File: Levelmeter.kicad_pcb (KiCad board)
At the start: 4 copper layers, 90 x 70 mm, 140 parts, among them J1 JST_PH_2.0mm_1x02, J2 USB_C, J4 Header_50mil_2x07, J5 Header_100mil_1x06, J6 Header_100mil_1x06, J7 JST_PH_2.0mm_1x03, Q1 DMG2305UX-13, Q2 FS8205A, Q3 DMG2305UX-13, Q4 AO3400A, Q5 AO3400A, SW1 PEC11R-4215F-S0024, SW2 PEC11R-4215F-S0024, U1 DW01A, U10 BME280, U11 SN74HC14PWR, U12 LM35, U13 SD6210A, U14 ADS131M04IPWR, U15 AD9833BRMZ-REEL7, U16 AD826ARZ-REEL7, U17 LM27761DSGR, U2 LP5907MFX-3.3/NOPB, U3 TP4056, U4 LP5907MFX-3.3/NOPB, U5 SD6210A, U6 STM32G0B1RET6, U7 RN4871-I/RM128, U8 SN74AHCT244DBR, U9 24LC256-I/ST, Y1 Q13FC1350000400, Y2 X50328MSB2GI

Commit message: Schematic and component placement semi-final. Routing pending
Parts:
- removed U13: SD6210A, sldrnrd:SOT-23-6
- added C54: 10u, sldrnrd:C_1206, F.Cu at (109.8, 83.0)
- added C55: 100n, sldrnrd:C_0603, F.Cu at (128.4, 41.2)
- added C56: 100n, sldrnrd:C_0603, F.Cu at (135.6, 45.6)
- added C57: 10u, sldrnrd:C_1206, F.Cu at (135.0, 55.6)
- added C58: 100n, sldrnrd:C_0603, F.Cu at (132.1, 62.7)
- added C59: 100n, sldrnrd:C_0603, F.Cu at (134.8, 60.2)
- added C60: 10n, sldrnrd:C_0603, F.Cu at (129.4, 60.8)
- added C61: 1n, sldrnrd:C_0603, F.Cu at (131.8, 52.6)
- added C62: 100p, sldrnrd:C_0603, F.Cu at (131.8, 51.0)
- added C63: 100n, sldrnrd:C_0603, F.Cu at (129.4, 57.6)
- added C64: 1u, sldrnrd:C_0603, F.Cu at (99.4, 41.4)
- added C65: 1u, sldrnrd:C_0603, F.Cu at (101.8, 34.0)
- added C66: 100n, sldrnrd:C_0603, F.Cu at (100.2, 34.0)
- added C67: 100n, sldrnrd:C_0603, F.Cu at (99.4, 43.0)
- added C68: 220n, sldrnrd:C_0603, F.Cu at (97.0, 42.2)
- added R33: 68k, sldrnrd:R_0603, F.Cu at (112.4, 90.0)
- added R35: 180k, sldrnrd:R_0603, F.Cu at (112.4, 88.4)
- added R38: 10k, sldrnrd:R_0603, F.Cu at (132.0, 38.8)
- added R49: 10k, sldrnrd:R_0603, F.Cu at (128.4, 45.2)
- added R50: 10k, sldrnrd:R_0805, F.Cu at (135.8, 42.2)
- added R51: 100k, sldrnrd:R_0805, F.Cu at (130.4, 48.4)
- added R52: 6k8, sldrnrd:R_0603, F.Cu at (129.4, 54.6)
- added R53: 68k, sldrnrd:R_0603, F.Cu at (129.4, 51.6)
- added R54: 10k, sldrnrd:R_0603, F.Cu at (131.8, 54.2)
- C42: value 100n -> 10u; footprint sldrnrd:C_0603 -> sldrnrd:C_1206
- C44: value 10u -> 100n; footprint sldrnrd:C_1206 -> sldrnrd:C_0603
- C45: value 2u2 -> 1u
- U16: value AD826ARZ-REEL7 -> AD826
- moved J5 117.0 mm to (62.0, 34.0), turned to 90 degrees
- moved R41 78.8 mm to (77.8, 37.2)
- moved R40 76.3 mm to (80.2, 38.0), turned to -90 degrees
- moved R43 74.7 mm to (82.6, 33.6)
- moved R42 71.6 mm to (85.0, 38.0), turned to -90 degrees
- moved U17 71.5 mm to (112.8, 84.6), turned to -90 degrees
- moved R39 69.2 mm to (87.4, 37.2)
- moved R32 67.6 mm to (85.6, 31.9)
- moved C50 66.3 mm to (82.6, 37.2)
- moved C47 66.2 mm to (82.5, 31.9)
- moved C51 62.8 mm to (89.8, 38.0), turned to -90 degrees
- moved C46 62.7 mm to (85.8, 33.6), turned to 180 degrees
- moved R48 58.3 mm to (102.6, 37.4), turned to 180 degrees
- moved U14 57.5 mm to (95.2, 36.4), turned to 180 degrees
- moved J6 56.0 mm to (128.0, 34.0), turned to -90 degrees
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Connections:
- C42 pad 1: VCC -> -4V5
- C44 pad 1: VCC -> -4V5
- C45 pad 1: Net-(U13-C+) -> Net-(U17-C1+)
- C45 pad 2: Net-(U13-C-) -> Net-(U17-C1-)
- J5 pad 1: unconnected-(J5-Pad1) -> 5V0
- J5 pad 2: unconnected-(J5-Pad2) -> -4V5
- J5 pad 3: unconnected-(J5-Pad3) -> GND
- J5 pad 4: unconnected-(J5-Pad4) -> ExciterA
- J5 pad 5: unconnected-(J5-Pad5) -> ExciterB
- J5 pad 6: unconnected-(J5-Pad6) -> Sensor1
- J6 pad 1: unconnected-(J6-Pad1) -> 5V0
- J6 pad 2: unconnected-(J6-Pad2) -> -4V5
- J6 pad 3: unconnected-(J6-Pad3) -> GND
- J6 pad 4: unconnected-(J6-Pad4) -> ExciterA
- J6 pad 5: unconnected-(J6-Pad5) -> ExciterB
- J6 pad 6: unconnected-(J6-Pad6) -> Sensor2
- U14 pad 1: unconnected-(U14-AVDD-Pad1) -> 3V3_Sensors
- U14 pad 10: ExciterB_ADC -> Sensor1_ADC
- U14 pad 11: unconnected-(U14-~{SYNC}/~{RESET}-Pad11) -> ADC_SYNC_RESET
- U14 pad 12: unconnected-(U14-~{CS}-Pad12) -> ADC_CS
- U14 pad 13: unconnected-(U14-~{DRDY}-Pad13) -> ADC_READY
- U14 pad 14: unconnected-(U14-SCLK-Pad14) -> ADC_SCK
- U14 pad 15: unconnected-(U14-DOUT-Pad15) -> ADC_MISO
- U14 pad 16: unconnected-(U14-DIN-Pad16) -> ADC_MOSI
- U14 pad 17: unconnected-(U14-CLKIN-Pad17) -> ADC_CLOCK
- U14 pad 18: unconnected-(U14-CAP-Pad18) -> Net-(U14-CAP)
- U14 pad 20: unconnected-(U14-DVDD-Pad20) -> 3V3_Sensors
- U14 pad 3: Sensor1_ADC -> Sensor2_ADC
- U14 pad 6: Sensor2_ADC -> ExciterB_ADC
- U15 pad 1: unconnected-(U15-COMP-Pad1) -> Net-(U15-COMP)
- U15 pad 10: unconnected-(U15-VOUT-Pad10) -> Net-(U15-VOUT)
- U15 pad 2: unconnected-(U15-VDD-Pad2) -> 3V3_Sensors
- U15 pad 3: unconnected-(U15-CAP/2.5V-Pad3) -> Net-(U15-CAP/2.5V)
- U15 pad 4: unconnected-(U15-DGND-Pad4) -> GND
- U15 pad 5: unconnected-(U15-MCLK-Pad5) -> DAC_Clock
- U15 pad 6: unconnected-(U15-SDATA-Pad6) -> DAC_MOSI
- U15 pad 7: unconnected-(U15-SCLK-Pad7) -> DAC_SCK
- U15 pad 8: unconnected-(U15-FSYNC-Pad8) -> DAC_FSYNC
- U15 pad 9: unconnected-(U15-AGND-Pad9) -> GND
- U16 pad 1: unconnected-(U16A-OUT1-Pad1) -> ExciterA
- U16 pad 2: unconnected-(U16A--IN1-Pad2) -> Net-(U16--IN1)
- U16 pad 3: unconnected-(U16A-+IN1-Pad3) -> SineSignal
- U16 pad 4: unconnected-(U16A-V--Pad4) -> -4V5
- U16 pad 5: unconnected-(U16B-+IN2-Pad5) -> GND
- U16 pad 6: unconnected-(U16B--IN2-Pad6) -> Net-(U16--IN2)
- U16 pad 7: unconnected-(U16B-OUT2-Pad7) -> ExciterB
- U16 pad 8: unconnected-(U16A-V+-Pad8) -> 5V0
- U17 pad 1: unconnected-(U17-VIN-Pad1) -> 5V0
- U17 pad 2: unconnected-(U17-GND-Pad2) -> GND
- U17 pad 3: unconnected-(U17-CPOUT-Pad3) -> Net-(U17-CPOUT)
- U17 pad 4: unconnected-(U17-VOUT-Pad4) -> -4V5
- U17 pad 5: unconnected-(U17-VFB-Pad5) -> Net-(U17-VFB)
- U17 pad 6: unconnected-(U17-EN-Pad6) -> 5V0
- U17 pad 7: unconnected-(U17-C1--Pad7) -> Net-(U17-C1-)
- U17 pad 8: unconnected-(U17-C1+-Pad8) -> Net-(U17-C1+)
- U17 pad 9: unconnected-(U17-EP-Pad9) -> GND
- U6 pad 1: BLE_P2_0 -> DAC_Clock
- U6 pad 13: PCAP04_2_SCL -> unconnected-(U6-PC0-Pad13)
- U6 pad 14: PCAP04_2_SDA -> unconnected-(U6-PC1-Pad14)
- U6 pad 15: PCAP04_2_P3 -> unconnected-(U6-PC2-Pad15)
- U6 pad 16: PCAP04_2_P2 -> ADC_SYNC_RESET
- U6 pad 18: PCAP04_2_INT -> ADC_READY
- U6 pad 2: ~{BLE_RST} -> DAC_MOSI
- U6 pad 21: SCL3300_CS -> ADC_CS
- U6 pad 22: SCL3300_SCK -> ADC_SCK
- U6 pad 23: SCL3300_MISO -> ADC_MISO
- U6 pad 24: SCL3300_MOSI -> ADC_MOSI
- U6 pad 3: BLE_P1_6 -> DAC_FSYNC
- U6 pad 30: unconnected-(U6-PB10-Pad30) -> ADC_CLOCK
- U6 pad 33: PCAP04_1_SCL -> unconnected-(U6-PB13-Pad33)
- U6 pad 34: PCAP04_1_SDA -> unconnected-(U6-PB14-Pad34)
- U6 pad 35: PCAP04_1_P3 -> unconnected-(U6-PB15-Pad35)
- U6 pad 36: PCAP04_1_P2 -> unconnected-(U6-PA8-Pad36)
- U6 pad 37: PCAP04_1_INT -> unconnected-(U6-PA9-Pad37)
- U6 pad 59: BLE_P1_7 -> ~{BLE_RST}
- U6 pad 64: BLE_P3_6 -> DAC_SCK
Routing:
- net 3V3_Sensors: track 97.3 -> 4.02 mm
- net 3V3: track 297.2 -> 223.9 mm
- net BLE_P2_0: track 51.9 -> 0.00 mm, vias 2 -> 0
- net ADC_CLOCK: track 0.00 -> 46.6 mm
- net BLE_P1_7: track 46.4 -> 0.00 mm, vias 2 -> 0
- net BLE_P1_6: track 41.0 -> 0.00 mm
- net PCAP04_2_SCL: track 38.3 -> 0.00 mm
- net BLE_P3_6: track 37.3 -> 0.00 mm
- net PCAP04_2_INT: track 35.4 -> 0.00 mm
- net PCAP04_2_SDA: track 33.4 -> 0.00 mm
- net PCAP04_2_P3: track 32.5 -> 0.00 mm
- net PCAP04_1_SCL: track 32.3 -> 0.00 mm
- net PCAP04_2_P2: track 32.0 -> 0.00 mm
- net PCAP04_1_SDA: track 32.0 -> 0.00 mm
- net PCAP04_1_INT: track 32.0 -> 0.00 mm
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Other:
- board text added: "soldernerd.com Levelmeter 2026 - Rev A"
- board text removed: "soldernerd.com 2026 - Rev A"

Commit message: Board layout without errors
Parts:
- removed the R46 at (109.8, 38.0)
- added R38: 10k, sldrnrd:R_0603, F.Cu at (79.4, 35.4)
- added R39: 10k, sldrnrd:R_0603, F.Cu at (112.3, 36.2)
- added R41: 10k, sldrnrd:R_0603, F.Cu at (113.9, 36.6)
- R40: value 5k1 -> 10k
- moved C17 10.9 mm to (108.2, 82.2), turned to 180 degrees
- moved C56 6.64 mm to (102.7, 39.4)
- moved R43 6.64 mm to (107.5, 39.4)
- moved R47 6.64 mm to (105.1, 38.6)
- moved C52 6.64 mm to (109.9, 38.6)
- moved R46 6.21 mm to (86.6, 38.0)
- moved C51 6.17 mm to (81.8, 38.0)
- moved C55 6.11 mm to (89.0, 38.8), turned to -90 degrees
- moved R42 5.44 mm to (84.2, 38.8), turned to -90 degrees
- moved R36 5.25 mm to (79.4, 32.2), turned to -90 degrees
- moved C18 4.67 mm to (112.8, 82.4)
- moved C50 4.47 mm to (132.8, 64.2), turned to 0 degrees
- moved R37 4.20 mm to (112.3, 33.0), turned to -90 degrees
- moved R40 3.54 mm to (77.8, 35.4)
- moved C54 3.20 mm to (109.9, 35.4)
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- renumbered C11 to C10, C7 to C11, C14 to C13, C15 to C14, C45 to C15, C54 to C16, C38 to C17, C40 to C18, C13 to C19, C42 to C20, C44 to C21, C16 to C22, C17 to C23, C18 to C24, C19 to C25, C20 to C26, C21 to C27, C22 to C28, C23 to C29, C4 to C3, C24 to C30, C25 to C31, C26 to C32, C27 to C33, C28 to C34, C29 to C35, C30 to C36, C31 to C37, C32 to C38, C33 to C39, C6 to C4, C34 to C40, C35 to C41, C36 to C42, C37 to C43, C39 to C44, C41 to C45, C43 to C46, C57 to C47, C58 to C48, C60 to C49, C3 to C5, C59 to C50, C47 to C51, C48 to C52, C50 to C53, C52 to C54, C46 to C55, C49 to C56, C51 to C57, C53 to C58, C63 to C59, C8 to C6, C61 to C60, C62 to C61, C66 to C62, C65 to C63, C67 to C65, C68 to C66, C56 to C67, C55 to C68, C9 to C7, C10 to C8, C5 to C9, J4 to J3, J7 to J4, Q3 to Q2, Q2 to Q3, R8 to R10, R9 to R11, R10 to R12, R11 to R13, R12 to R14, R13 to R15, R14 to R16, R15 to R17, R16 to R18, R17 to R19, R18 to R20, R19 to R21, R20 to R22, R21 to R23, R22 to R24, R23 to R25, R24 to R26, R25 to R27, R26 to R28, R27 to R29, R28 to R30, R29 to R31, R30 to R32, R31 to R33, R37 to R35, R41 to R36, R45 to R37, R43 to R42, R44 to R43, R42 to R44, R47 to R45, R32 to R46, R36 to R47, R39 to R48, R48 to R49, R54 to R50, R52 to R51, R53 to R52, R51 to R53, R50 to R54, R49 to R55, R38 to R56, R35 to R8, R33 to R9, U2 to U1, U9 to U10, U10 to U11, U11 to U12, U12 to U13, U15 to U14, U14 to U15, U1 to U2, U4 to U3, U3 to U4, U17 to U6, U6 to U7, U7 to U8, U8 to U9
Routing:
- net 5V0: track 90.3 -> 292.4 mm, vias 5 -> 12
- net -4V5: track 5.13 -> 184.0 mm, vias 0 -> 6
- net ExciterA: track 0.00 -> 87.2 mm
- net ExciterB: track 0.00 -> 79.1 mm
- net 3V3_Sensors: track 4.02 -> 78.1 mm, vias 0 -> 4
- net 3V3: track 223.9 -> 269.9 mm, vias 20 -> 22
- net DAC_SCK: track 20.6 -> 59.8 mm
- net DAC_Clock: track 19.9 -> 51.0 mm
- net DAC_MOSI: track 19.0 -> 48.1 mm
- net DAC_FSYNC: track 18.8 -> 46.8 mm, vias 0 -> 2
- net VCC: track 112.5 -> 128.4 mm
- net Sensor1: track 0.00 -> 10.2 mm
- net ExciterB_ADC: track 7.37 -> 17.3 mm
- net Sensor2: track 0.00 -> 9.93 mm
- net Sensor2_ADC: track 7.62 -> 17.3 mm
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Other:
- board text added: "+5"
- board text added: "-5"
- board text added: "A"
- board text added: "B"
- board text added: "GND"
- board text added: "S1"
- board text added: "S2"

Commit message: Unavailable parts replaced, rotation issues fixed in library, except for U7
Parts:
- Q3: footprint sldrnrd:TSSOP-8 -> sldrnrd:SOT-23-6
- R2: value 2k -> 1k
- R3: value 1k -> 470R
- moved J6 6.35 mm to (121.7, 33.1), turned to 180 degrees
- moved J5 6.35 mm to (68.3, 33.0), turned to 0 degrees
- moved J4 2.00 mm to (61.7, 95.2), turned to -90 degrees
- moved J1 0.99 mm to (137.3, 74.7), turned to 90 degrees
- moved Q3 0.46 mm to (123.6, 69.9), turned to -90 degrees
- moved U2 0.15 mm to (127.1, 70.1), turned to 90 degrees
- turned U5 to 90 degrees
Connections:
- Q3 pad 1: unconnected-(Q3-D-Pad1) -> BAT-
- Q3 pad 2: BAT- -> unconnected-(Q3-D-Pad2)
- Q3 pad 3: BAT- -> GND
- Q3 pad 4: Net-(Q3-G1) -> Net-(Q3-G2)
- Q3 pad 5: Net-(Q3-G2) -> unconnected-(Q3-D-Pad5)
- Q3 pad 6: GND -> Net-(Q3-G1)
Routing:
- net Net-(Q3-G1): track 7.73 -> 1.62 mm
- net GND: track 11.0 -> 14.7 mm, vias 280 -> 292
- net BAT-: track 30.1 -> 26.8 mm
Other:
- board text added: "+5V"
- board text added: "-5V"
- board text added: "soldernerd.com LEVELMETER 2026 - Rev A"
- board text removed: "+5"
- board text removed: "-5"
- board text removed: "soldernerd.com Levelmeter 2026 - Rev A"

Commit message: Fix stock/pinout issues, re-export fabrication files, apply JLC rotation corrections
- Replace out-of-stock parts (D2/D3 LED, U5, U10) with in-stock JLCPCB
  alternatives; add D5-D12 protection diodes
- Fix U2/DW01A footprint rotation on PCB
- Re-export gerbers, drill files, and JLCSMT BOM/CPL from current design
- BOM/CPL: DS1 uses header connector LCSC number only (display bought
  separately), U13 (LM35) and mounting holes excluded as do-not-place
- CPL rotations for U7, U5, Q3, U2 corrected per known JLCPCB
  per-part orientation quirks (see sldrnrd_kicad_lib/JLC_ROTATION_OFFSETS.md)
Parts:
- added D10: 1N4148WS, sldrnrd:SOD-323, F.Cu at (121.8, 45.6)
- added D11: 1N4148WS, sldrnrd:SOD-323, F.Cu at (118.4, 43.6)
- added D12: 1N4148WS, sldrnrd:SOD-323, F.Cu at (121.8, 43.6)
- added D5: 1N4148WS, sldrnrd:SOD-323, F.Cu at (71.4, 46.2)
- added D6: 1N4148WS, sldrnrd:SOD-323, F.Cu at (74.8, 46.2)
- added D7: 1N4148WS, sldrnrd:SOD-323, F.Cu at (71.4, 44.0)
- added D8: 1N4148WS, sldrnrd:SOD-323, F.Cu at (74.8, 44.0)
- added D9: 1N4148WS, sldrnrd:SOD-323, F.Cu at (118.4, 45.6)
- U10: value 24LC256-I/ST -> BL24C256A-SFRC
- U5: value SD6210A -> HX4002-MFC
- moved D1 0.10 mm to (69.5, 82.6), turned to 90 degrees
- moved D2 0.10 mm to (71.2, 82.6), turned to 90 degrees
- turned D3 to 0 degrees
- turned D4 to 0 degrees
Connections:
- D1 pad 1: 3V3 -> Net-(D1-K)
- D1 pad 2: Net-(D1-K) -> 3V3
- D2 pad 1: 3V3 -> Net-(D2-K)
- D2 pad 2: Net-(D2-K) -> 3V3
- D3 pad 1: Net-(D3-A) -> GND
- D3 pad 2: GND -> Net-(D3-K)
- D4 pad 1: Net-(D4-A) -> GND
- D4 pad 2: GND -> Net-(D4-K)
- R12 pad 2: Net-(D3-A) -> Net-(D3-K)
- R13 pad 2: Net-(D4-A) -> Net-(D4-K)
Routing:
- net Net-(D11-A): track 3.22 -> 16.9 mm
- net Net-(D6-K): track 3.22 -> 15.4 mm
- net Net-(D4-K): track 0.00 -> 1.64 mm
- net Net-(D4-A): track 1.64 -> 0.00 mm
- net Net-(D3-K): track 0.00 -> 1.64 mm
- net Net-(D3-A): track 1.64 -> 0.00 mm
- net Net-(SW2-SW1): track 24.7 -> 26.2 mm
- net Net-(D7-A): track 0.00 -> 1.30 mm
- net Net-(D5-K): track 0.00 -> 1.30 mm
- net Net-(D11-K): track 0.00 -> 1.30 mm
- net Net-(D10-K): track 0.00 -> 1.30 mm
- net GND: vias 292 -> 294

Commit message: Semi-final, including fabrication files
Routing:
- net LED_PWR: track 12.6 -> 10.3 mm, vias 2 -> 0
- net LED_STATUS: track 13.2 -> 11.8 mm, vias 2 -> 0

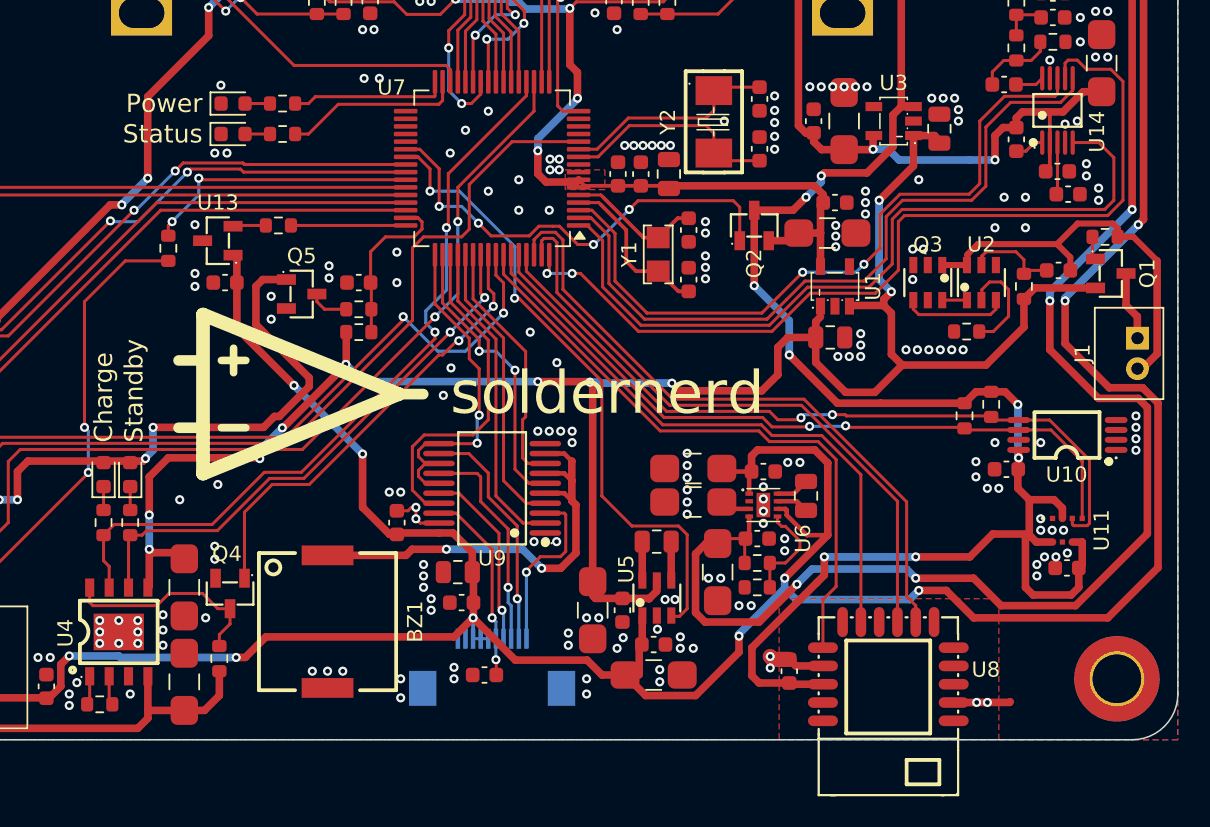
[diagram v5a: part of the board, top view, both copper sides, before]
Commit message: Header for external BME280 module added, Keepout for BLE module fixed
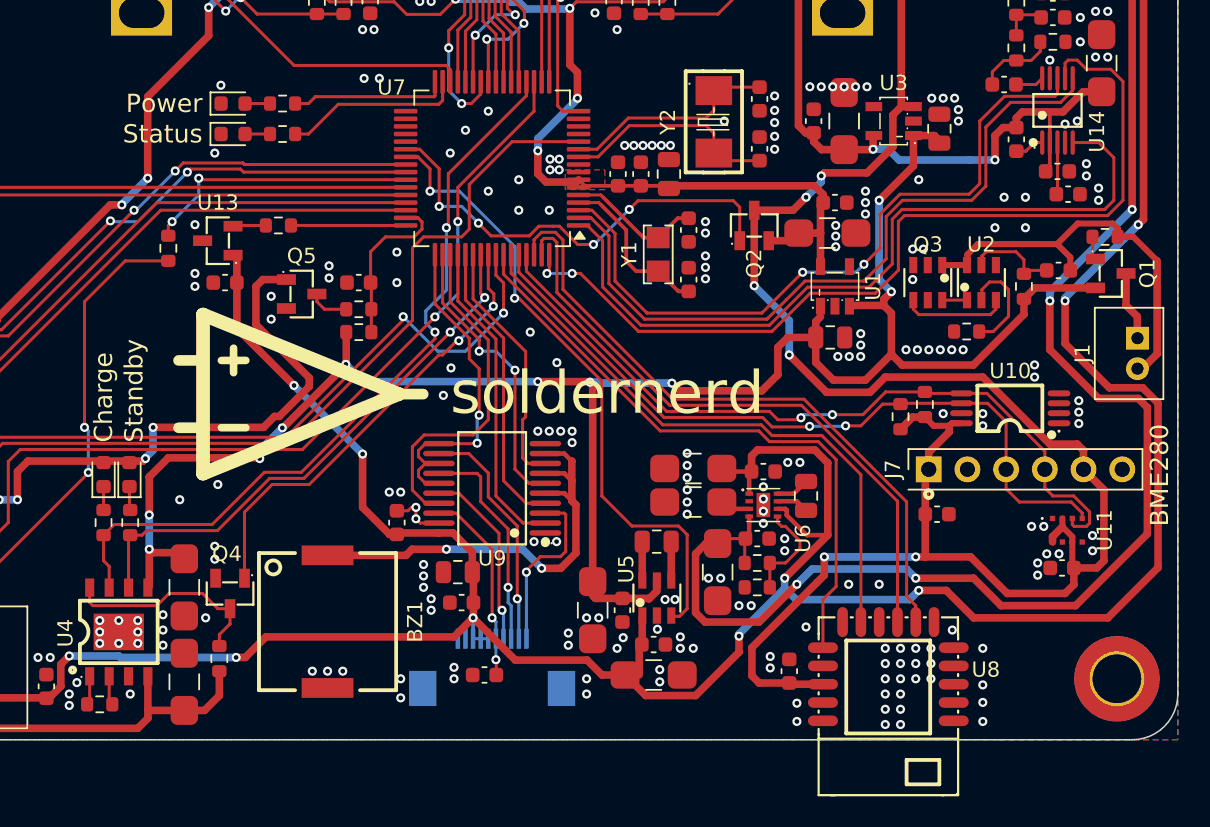
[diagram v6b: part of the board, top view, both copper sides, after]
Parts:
- added J7: Header_100mil_1x06, sldrnrd:Header_100mil_1x06, F.Cu at (130.0, 82.2)
- moved C32 5.42 mm to (124.2, 85.2), turned to 0 degrees
- moved R20 4.35 mm to (123.4, 78.0), turned to 90 degrees
- moved R21 4.20 mm to (121.8, 78.8), turned to 90 degrees
- moved U10 4.14 mm to (129.0, 78.2)
- moved C40 0.32 mm to (132.4, 88.7)
- turned D2 to -90 degrees
- turned D1 to -90 degrees
- turned D3 to 180 degrees
- turned D4 to 180 degrees
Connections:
- U11 pad 5: 3V3 -> GND
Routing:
- net 3V3: track 269.9 -> 283.6 mm, vias 22 -> 20
- net GND: track 14.7 -> 7.19 mm, vias 294 -> 316
- net EEPROM_SCL: track 47.1 -> 49.0 mm
- net VCC: track 128.4 -> 126.8 mm
- net EEPROM_SDA: track 49.2 -> 49.9 mm
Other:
- board text added: "BME280"

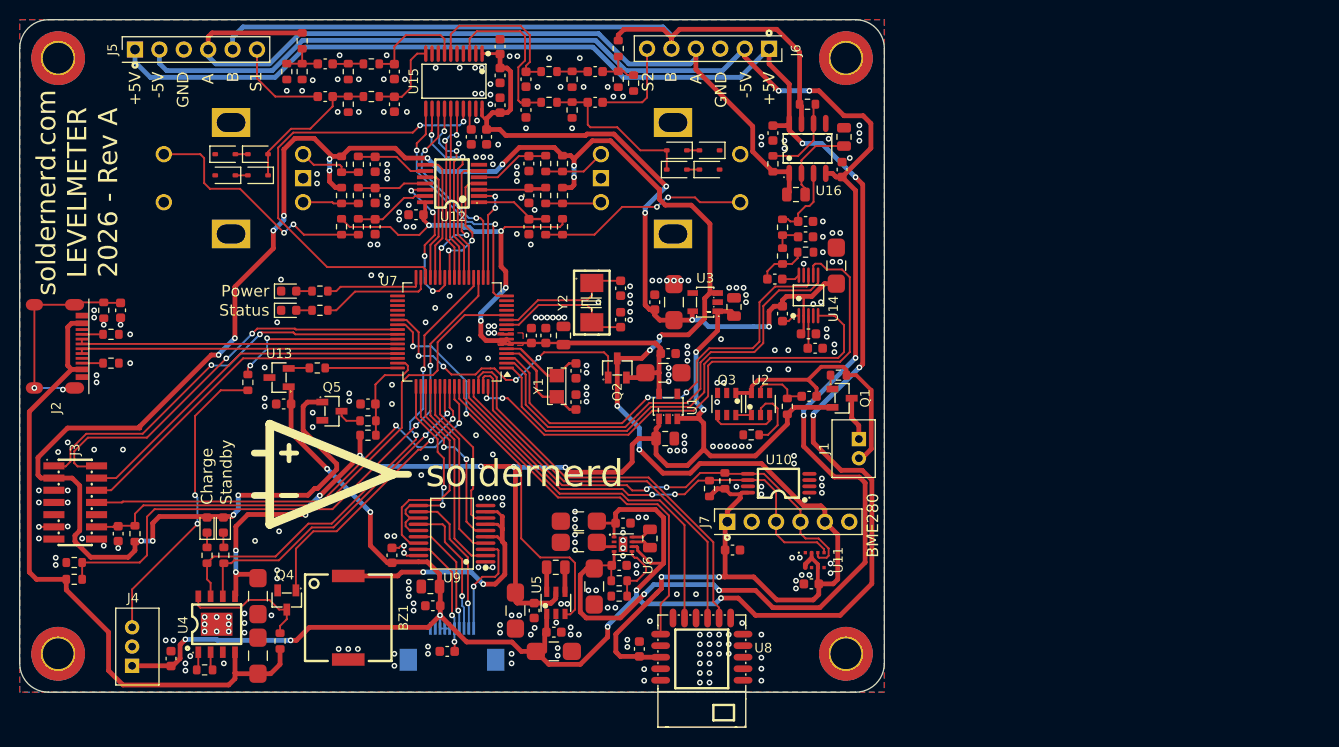
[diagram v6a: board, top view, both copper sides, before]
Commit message: BLE module: footprint fixed (keepout areas), additional pins routed to MCU, 3-pin 50mil debug header added
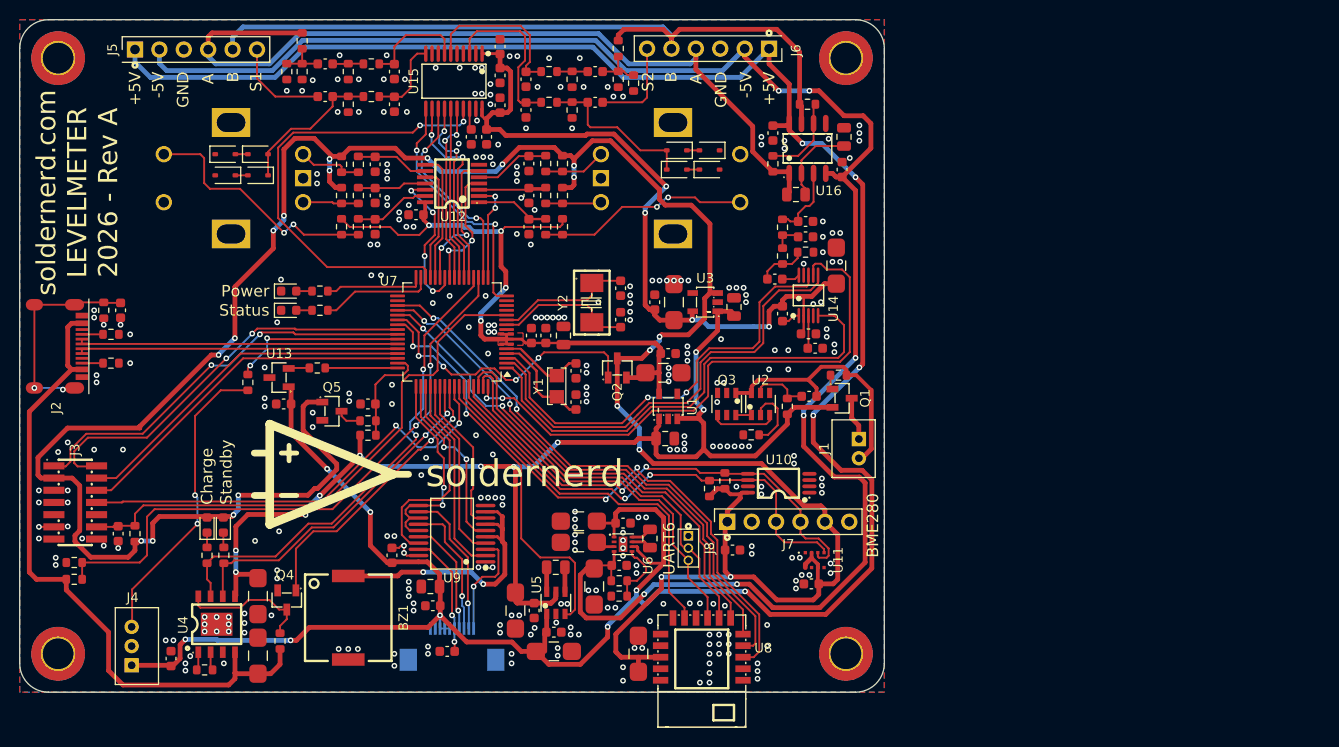
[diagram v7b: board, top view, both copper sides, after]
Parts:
- added J8: Header_100mil_1x02, sldrnrd:Header_50mil_1x03, F.Cu at (119.6, 85.0)
- C29: value 100n -> 10u; footprint sldrnrd:C_0603 -> sldrnrd:C_1206
- moved C29 0.51 mm to (114.4, 96.0)
- moved J4 0.07 mm to (61.6, 95.2)
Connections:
- U7 pad 35: unconnected-(U7-PB15-Pad35) -> BLE_P1_3
- U7 pad 36: unconnected-(U7-PA8-Pad36) -> BLE_P1_7
- U7 pad 37: unconnected-(U7-PA9-Pad37) -> BLE_P1_6
- U7 pad 58: BLE_P0_2 -> BLE_P1_2
- U8 pad 11: unconnected-(U8-P0_0-Pad11) -> BLE_P0_0
- U8 pad 15: unconnected-(U8-P2_7-Pad15) -> BLE_P2_7
- U8 pad 3: unconnected-(U8-P1_2-Pad3) -> BLE_P1_2
- U8 pad 4: unconnected-(U8-P1_3-Pad4) -> BLE_P1_3
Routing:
- net BLE_P1_3: track 0.00 -> 58.5 mm, vias 0 -> 2
- net BLE_P1_7: track 0.00 -> 55.0 mm, vias 0 -> 2
- net BLE_P1_2: track 0.00 -> 53.2 mm, vias 0 -> 2
- net BLE_P1_6: track 0.00 -> 52.5 mm, vias 0 -> 2
- net BLE_P0_2: track 40.8 -> 0.00 mm
- net VCC: track 126.8 -> 124.5 mm
- net 3V3: track 283.6 -> 284.5 mm
- net 3V3_STANDBY: track 68.0 -> 68.9 mm
- net EEPROM_SCL: track 49.0 -> 49.7 mm
- net EEPROM_SDA: track 49.9 -> 50.5 mm
- net GND: vias 316 -> 314
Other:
- board text added: "UART6"
